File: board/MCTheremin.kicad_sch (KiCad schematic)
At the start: 94 parts, among them J1 Barrel_Jack, J11 Conn_01x01, J12 Conn_01x01, J14 Conn_01x01, J15 Conn_01x01, J2 Conn_01x02, J21 DIN-5_180degree, J3 AudioJack2_Dual_Ground_Switch, J4 AudioJack2_Dual_Ground_Switch, J5 Conn_01x02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

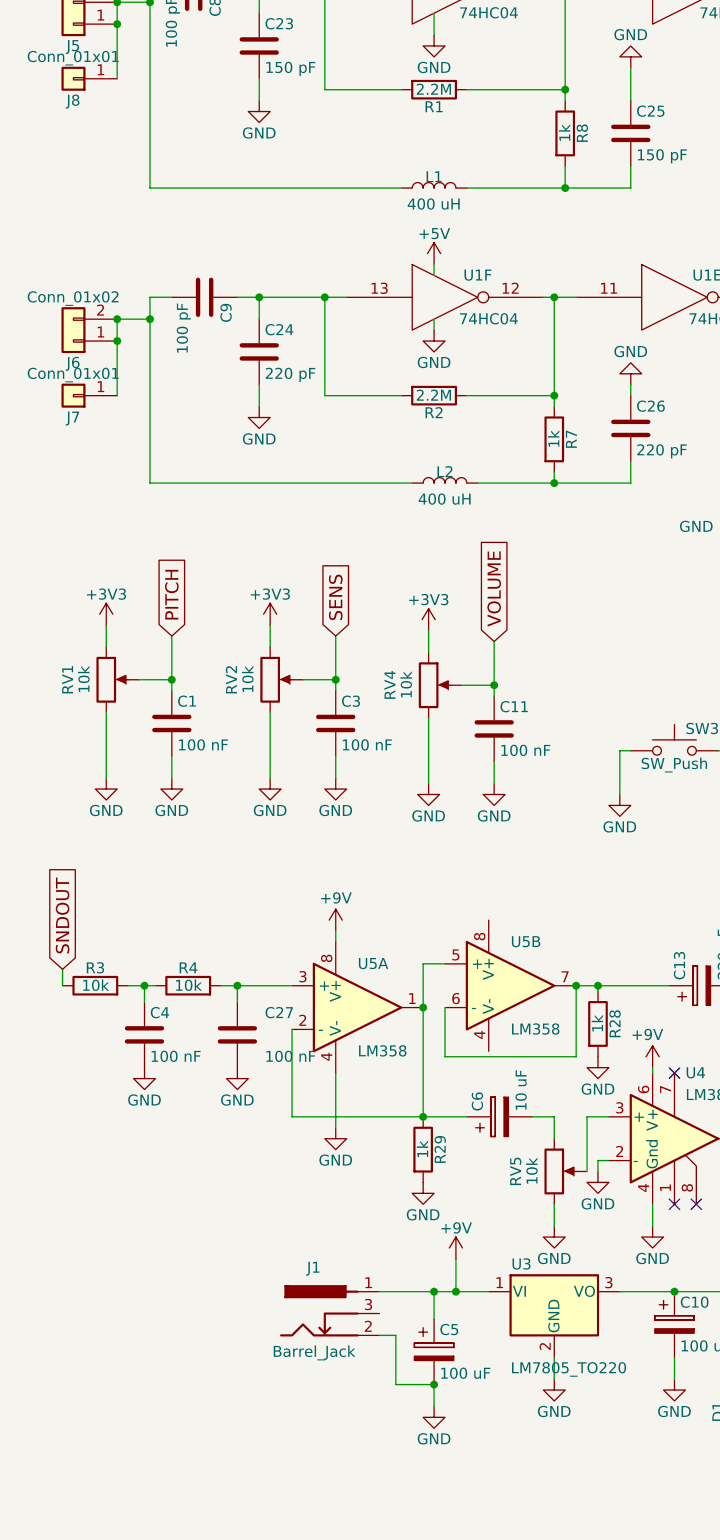
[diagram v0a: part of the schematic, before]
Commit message: Added external inductor support
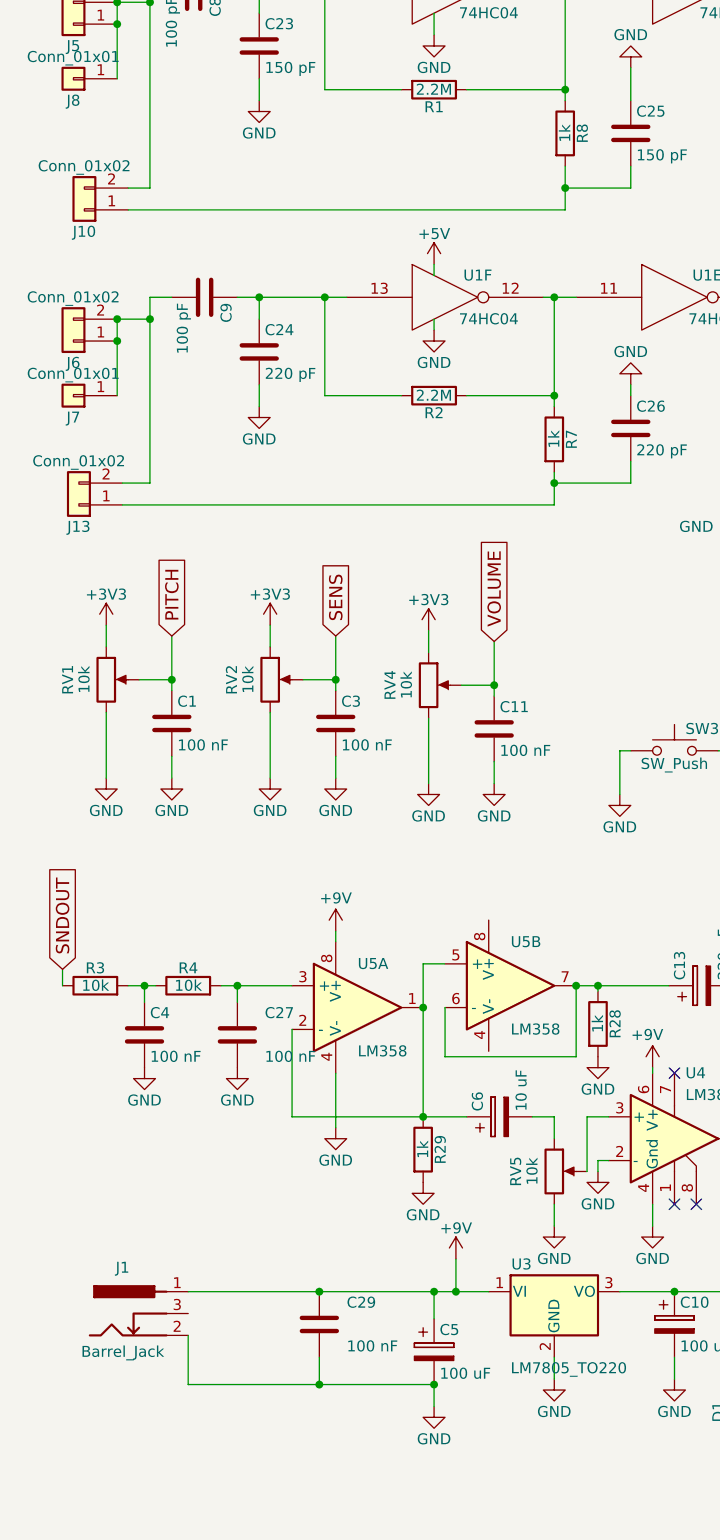
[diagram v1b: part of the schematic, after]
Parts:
- removed L1, L2: 400 uH, Inductors_THT:L_Axial_L7.0mm_D3.3mm_P12.70mm_Horizontal_Fastron_MICC, symbol MCTheremin-rescue:L
- added C29: 100 nF, Capacitor_THT:C_Disc_D5.0mm_W2.5mm_P5.00mm, symbol MCTheremin-rescue:C
- added J10, J13: Conn_01x02, TerminalBlock:TerminalBlock_bornier-2_P5.08mm, symbol MCTheremin-rescue:Conn_01x02
- D1: footprint LEDs:LED_D5.0mm -> LED_THT:LED_D5.0mm
- J5: footprint Connectors_Terminal_Blocks:TerminalBlock_bornier-2_P5.08mm -> TerminalBlock:TerminalBlock_bornier-2_P5.08mm
- R12, R13, R5: footprint Resistors_THT:R_Axial_DIN0207_L6.3mm_D2.5mm_P7.62mm_Horizontal -> Resistor_THT:R_Axial_DIN0207_L6.3mm_D2.5mm_P7.62mm_Horizontal
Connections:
- net +9V: now also C29.1
- net GND: now also C29.2
- net at C8.2, J5.1 (Pin_1), J5.2 (Pin_2)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: now also J10.2 (Pin_2)
- net at C9.2, J6.1 (Pin_1), J6.2 (Pin_2)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: now also J13.2 (Pin_2)
- net at C25.2, R8.2: now also J10.1 (Pin_1)
- net at C26.2, R7.2: now also J13.1 (Pin_1)
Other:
- moved on the sheet: J1

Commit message: Fixed layout
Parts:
- added R10, R15, R37, R38, R39: 2k, Resistor_THT:R_Axial_DIN0207_L6.3mm_D2.5mm_P7.62mm_Horizontal, symbol MCTheremin-rescue:R
- added R17, R35, R36: 1k, Resistor_THT:R_Axial_DIN0207_L6.3mm_D2.5mm_P7.62mm_Horizontal, symbol MCTheremin-rescue:R
- C27, C4: value 100 nF -> 10 nF
- R3, R4: value 10k -> 1k
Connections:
- net GND: now also R10.1
- net SNDOUT: now also R36.1, R39.1; no longer U7.14 (GPIO10)
- net at C24.1, C9.1, R2.2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: now also J13.2 (Pin_2)
- net at C8.2, J5.1 (Pin_1), J5.2 (Pin_2)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: no longer J10.2 (Pin_2)
- net at C9.2, J6.1 (Pin_1), J6.2 (Pin_2)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: no longer J13.2 (Pin_2)
- net at C23.1, C8.1, R1.2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: now also J10.2 (Pin_2)
- net at U7.15 (GPIO11): now also R37.2
- net at U7.16 (GPIO12): now also R38.2
- net at U7.17 (GPIO13): now also R39.2
- new net: R10.2, R15.1, R17.2
- new net: R35.1, R36.2, R38.1
- new net: R15.2, U7.14 (GPIO10)
- new net: R17.1, R35.2, R37.1
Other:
- moved on the sheet: C23, C24, J5, J6, J7, J8
